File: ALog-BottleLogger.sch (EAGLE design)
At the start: 98 parts, among them IC2 ATMEGA644M, J6 5.5x2.1mm Barrel, Q1 220mA/50V/3.5Ω, Q4 4.3A/20V/54mΩ, Q5 4.3A/20V/54mΩ, Q6 4.3A/20V/54mΩ, Q7 4.3A/20V/54mΩ, Q8 220mA/50V/3.5Ω, Q9 220mA/50V/3.5Ω, U2 FT231X-Q

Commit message: fully routed, looking for review
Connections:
- net +3V3: no longer J14.2
- net 1.8V_REF: no longer J14.1
- net ADC10: now also J14.10; no longer J15.2
- net ADC11: now also J14.9; no longer J15.1
- net ADC12: now also J14.5; no longer J14.7
- net ADC13: now also J14.4; no longer J14.6
- net ADC8: now also J15.5; no longer J15.7
- net ADC9: now also J15.4; no longer J15.6
- net BATT+: now also J2.9
- net D15~: now also J2.8; no longer J2.10
- net D3~: now also J2.6; no longer J2.8
- net EXT_3.3V: now also J14.2, J14.7, J15.2, J15.7, J2.4; no longer J14.4, J14.9, J15.4, J15.9, J2.6
- net EXT_5V: now also J14.8, J15.8, J2.5; no longer J14.10, J15.10, J2.7
- net EXT_5V1: now also J14.3, J15.3; no longer J14.5, J15.5
- net GND: now also J14.1, J14.6, J15.1, J15.6, J2.10, J2.3; no longer J14.3, J14.8, J15.3, J15.8, J2.5
- net MCU_ADC0: now also J2.7; no longer J2.9
- net MISO/D6: now also J15.10; no longer J2.2
- net MOSI/D5: now also J2.1; no longer J2.3
- net SCK/D7: now also J15.9; no longer J2.1
- net SS/D4: now also J2.2; no longer J2.4

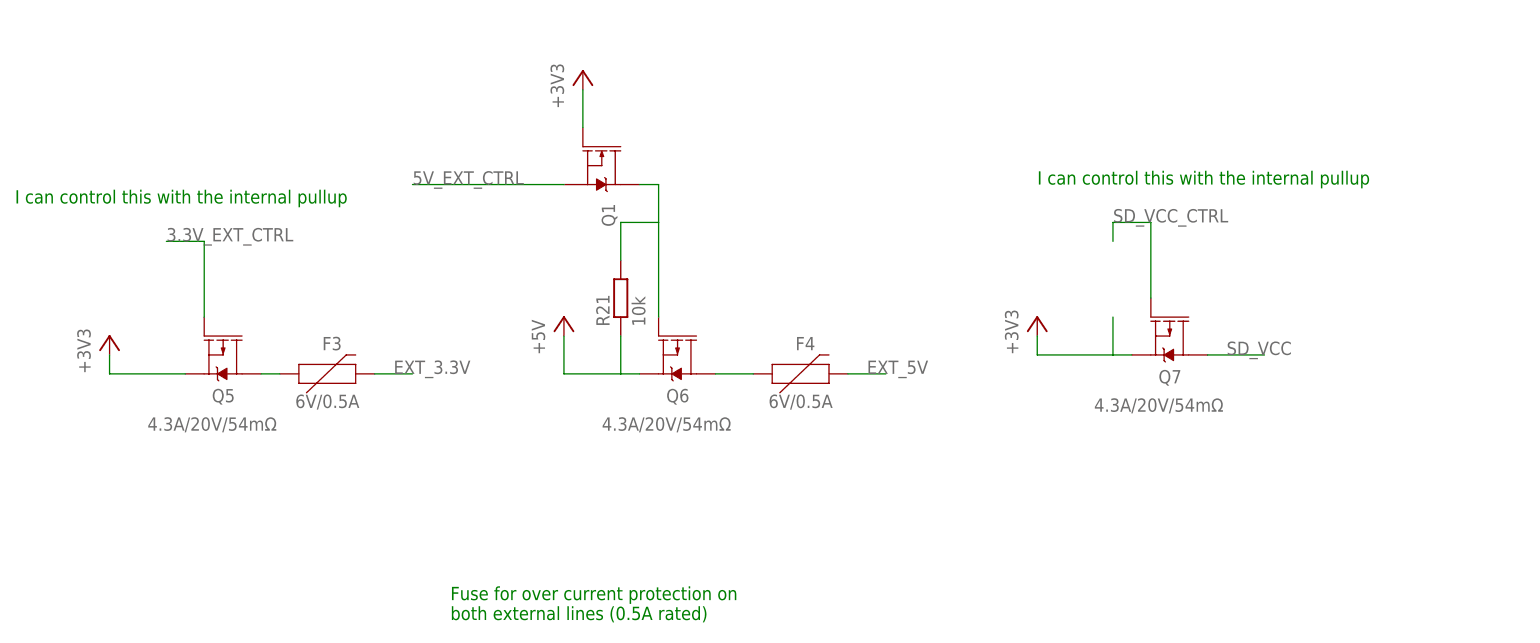
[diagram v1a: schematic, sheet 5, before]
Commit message: Add 10K pull downs on mosphets for external controls
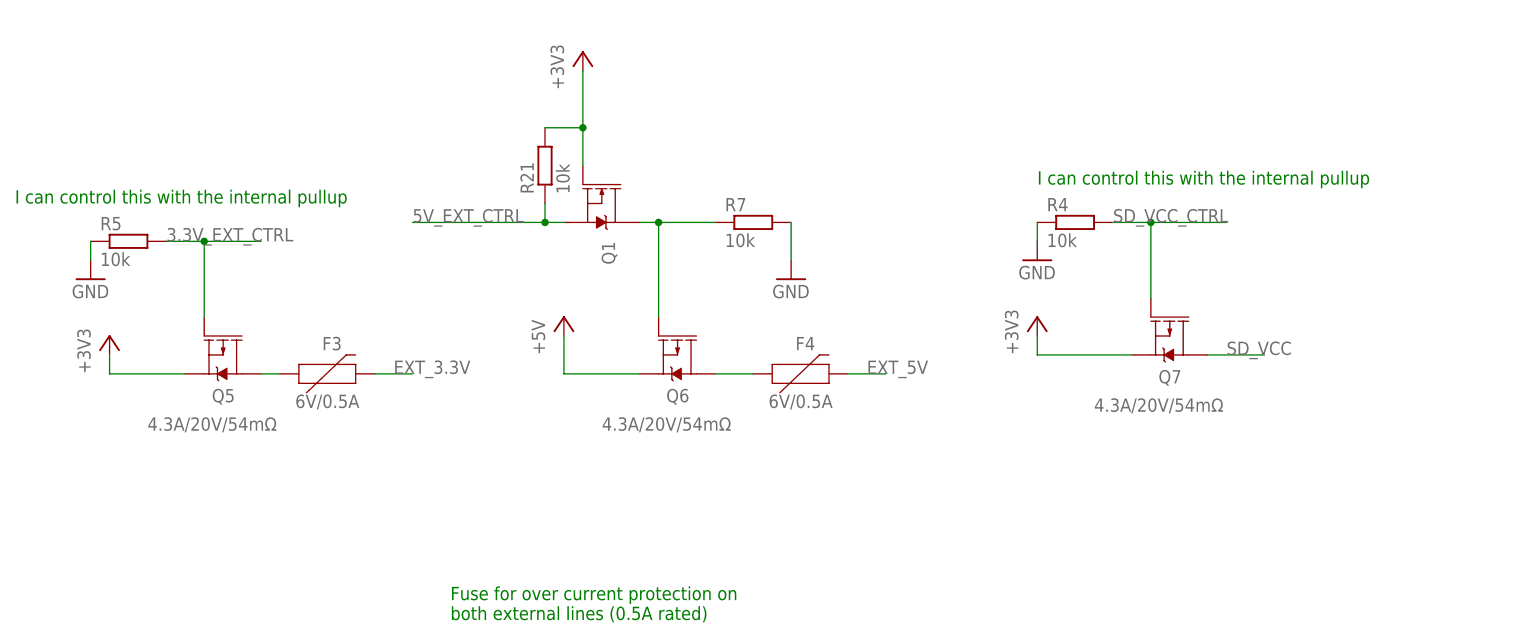
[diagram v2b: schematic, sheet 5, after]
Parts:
- added R4, R5, R7: 10k, rcl:R-EU_R0603
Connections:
- net +3V3: now also R21.2
- net +5V: no longer R21.1
- net 3.3V_EXT_CTRL: now also R5.2
- net 5V_EXT_CTRL: now also R21.1
- net GND: now also R7.2
- net SDA_HV: now also R7.1; no longer R21.2
- net SD_VCC_CTRL: now also R4.2
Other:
- moved on the sheet: Q1, R21
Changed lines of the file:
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@@
 <part name="R_LED1" library="resistor" deviceset="R-US_" device="R0603" value="220"/>
 <part name="GND11" library="supply1" deviceset="GND" device=""/>
+<part name="R4" library="rcl" deviceset="R-EU_" device="R0603" value="10k"/>
+<part name="R5" library="rcl" deviceset="R-EU_" device="R0603" value="10k"/>
+<part name="GND13" library="supply1" deviceset="GND" device=""/>
+<part name="GND14" library="supply1" deviceset="GND" device=""/>
+<part name="GND17" library="supply1" deviceset="GND" device=""/>
+<part name="R7" library="rcl" deviceset="R-EU_" device="R0603" value="10k"/>
 </parts>
 <sheets>
@@
 <attribute name="VALUE" x="58.42" y="27.94" size="1.778" layer="96" font="vector"/>
 </instance>
-<instance part="R21" gate="G$1" x="60.96" y="45.72" rot="R90"/>
+<instance part="R21" gate="G$1" x="50.8" y="63.5" rot="R90"/>
 <instance part="F3" gate="G$1" x="20.32" y="35.56"/>
 <instance part="F4" gate="G$1" x="83.82" y="35.56"/>
 <instance part="P+1" gate="1" x="53.34" y="43.18"/>
-<instance part="Q1" gate="NMOS" x="58.42" y="63.5" smashed="yes" rot="R270">
-<attribute name="NAME" x="58.42" y="58.42" size="1.778" layer="95" font="vector" rot="R270"/>
+<instance part="Q1" gate="NMOS" x="58.42" y="58.42" smashed="yes" rot="R270">
+<attribute name="NAME" x="58.42" y="53.34" size="1.778" layer="95" font="vector" rot="R270"/>
 </instance>
-<instance part="+3V12" gate="G$1" x="55.88" y="76.2"/>
+<instance part="+3V12" gate="G$1" x="55.88" y="78.74"/>
 <instance part="+3V13" gate="G$1" x="116.84" y="43.18"/>
 <instance part="+3V14" gate="G$1" x="-7.62" y="40.64"/>
+<instance part="R4" gate="G$1" x="121.92" y="55.88"/>
+<instance part="R5" gate="G$1" x="-5.08" y="53.34"/>
+<instance part="GND13" gate="1" x="-10.16" y="48.26"/>
+<instance part="GND14" gate="1" x="116.84" y="50.8"/>
+<instance part="GND17" gate="1" x="83.82" y="48.26"/>
+<instance part="R7" gate="G$1" x="78.74" y="55.88"/>
 </instances>
 <busses>
@@
 <net name="SD_VCC_CTRL" class="0">
 <segment>
-<wire x1="127" y1="53.34" x2="127" y2="55.88" width="0.1524" layer="91"/>
 <pinref part="Q7" gate="G$1" pin="G"/>
 <wire x1="127" y1="55.88" x2="132.08" y2="55.88" width="0.1524" layer="91"/>
 <wire x1="132.08" y1="55.88" x2="132.08" y2="45.72" width="0.1524" layer="91"/>
 <label x="127" y="55.88" size="1.778" layer="95"/>
+<pinref part="R4" gate="G$1" pin="2"/>
+<wire x1="132.08" y1="55.88" x2="142.24" y2="55.88" width="0.1524" layer="91"/>
+<junction x="132.08" y="55.88"/>
 </segment>
 </net>
@@
 <wire x1="5.08" y1="53.34" x2="5.08" y2="43.18" width="0.1524" layer="91"/>
 <label x="0" y="53.34" size="1.778" layer="95"/>
+<pinref part="R5" gate="G$1" pin="2"/>
+<wire x1="5.08" y1="53.34" x2="12.7" y2="53.34" width="0.1524" layer="91"/>
+<junction x="5.08" y="53.34"/>
 </segment>
 </net>
@@
 <segment>
 <pinref part="Q6" gate="G$1" pin="S"/>
-<wire x1="63.5" y1="35.56" x2="60.96" y2="35.56" width="0.1524" layer="91"/>
-<pinref part="R21" gate="G$1" pin="1"/>
-<wire x1="60.96" y1="35.56" x2="53.34" y2="35.56" width="0.1524" layer="91"/>
+<wire x1="63.5" y1="35.56" x2="53.34" y2="35.56" width="0.1524" layer="91"/>
 <wire x1="53.34" y1="35.56" x2="53.34" y2="40.64" width="0.1524" layer="91"/>
-<wire x1="60.96" y1="40.64" x2="60.96" y2="35.56" width="0.1524" layer="91"/>
 <pinref part="P+1" gate="1" pin="+5V"/>
 </segment>
@@
 <segment>
 <pinref part="Q1" gate="NMOS" pin="D"/>
-<wire x1="63.5" y1="60.96" x2="66.04" y2="60.96" width="0.1524" layer="91"/>
+<wire x1="63.5" y1="55.88" x2="66.04" y2="55.88" width="0.1524" layer="91"/>
 <pinref part="Q6" gate="G$1" pin="G"/>
-<wire x1="66.04" y1="60.96" x2="66.04" y2="55.88" width="0.1524" layer="91"/>
+<wire x1="66.04" y1="55.88" x2="66.04" y2="43.18" width="0.1524" layer="91"/>
+<junction x="66.04" y="55.88"/>
+<pinref part="R7" gate="G$1" pin="1"/>
+<wire x1="66.04" y1="55.88" x2="73.66" y2="55.88" width="0.1524" layer="91"/>
+</segment>
+</net>
+<net name="+3V3" class="0">
+<segment>
+<pinref part="Q1" gate="NMOS" pin="G"/>
+<wire x1="55.88" y1="76.2" x2="55.88" y2="68.58" width="0.1524" layer="91"/>
+<pinref part="+3V12" gate="G$1" pin="+3V3"/>
 <pinref part="R21" gate="G$1" pin="2"/>
-<wire x1="66.04" y1="55.88" x2="66.04" y2="43.18" width="0.1524" layer="91"/>
-<wire x1="60.96" y1="50.8" x2="60.96" y2="55.88" width="0.1524" layer="91"/>
-<wire x1="60.96" y1="55.88" x2="66.04" y2="55.88" width="0.1524" layer="91"/>
-</segment>
-</net>
-<net name="+3V3" class="0">
-<segment>
-<pinref part="Q1" gate="NMOS" pin="G"/>
-<wire x1="55.88" y1="73.66" x2="55.88" y2="68.58" width="0.1524" layer="91"/>
-<pinref part="+3V12" gate="G$1" pin="+3V3"/>
+<wire x1="55.88" y1="68.58" x2="55.88" y2="63.5" width="0.1524" layer="91"/>
+<wire x1="50.8" y1="68.58" x2="55.88" y2="68.58" width="0.1524" layer="91"/>
+<junction x="55.88" y="68.58"/>
 </segment>
 <segment>
 <pinref part="Q7" gate="G$1" pin="S"/>
-<wire x1="129.54" y1="38.1" x2="127" y2="38.1" width="0.1524" layer="91"/>
-<wire x1="127" y1="38.1" x2="116.84" y2="38.1" width="0.1524" layer="91"/>
-<wire x1="127" y1="43.18" x2="127" y2="38.1" width="0.1524" layer="91"/>
+<wire x1="129.54" y1="38.1" x2="116.84" y2="38.1" width="0.1524" layer="91"/>
 <wire x1="116.84" y1="40.64" x2="116.84" y2="38.1" width="0.1524" layer="91"/>
 <pinref part="+3V13" gate="G$1" pin="+3V3"/>
@@
 <segment>
 <pinref part="Q1" gate="NMOS" pin="S"/>
-<wire x1="53.34" y1="60.96" x2="33.02" y2="60.96" width="0.1524" layer="91"/>
-<label x="33.02" y="60.96" size="1.778" layer="95"/>
-</segment>
-</net>
+<wire x1="53.34" y1="55.88" x2="50.8" y2="55.88" width="0.1524" layer="91"/>
+<label x="33.02" y="55.88" size="1.778" layer="95"/>
+<pinref part="R21" gate="G$1" pin="1"/>
+<wire x1="50.8" y1="55.88" x2="33.02" y2="55.88" width="0.1524" layer="91"/>
+<wire x1="50.8" y1="58.42" x2="50.8" y2="55.88" width="0.1524" layer="91"/>
+<junction x="50.8" y="55.88"/>
+</segment>
+</net>
+<net name="GND" class="0">
+<segment>
+<pinref part="GND13" gate="1" pin="GND"/>
+<wire x1="-10.16" y1="53.34" x2="-10.16" y2="50.8" width="0.1524" layer="91"/>
+</segment>
+<segment>
+<pinref part="GND14" gate="1" pin="GND"/>
+<wire x1="116.84" y1="55.88" x2="116.84" y2="53.34" width="0.1524" layer="91"/>
+</segment>
+<segment>
+<pinref part="GND17" gate="1" pin="GND"/>
+<pinref part="R7" gate="G$1" pin="2"/>
+<wire x1="83.82" y1="55.88" x2="83.82" y2="50.8" width="0.1524" layer="91"/>
+</segment>
+</net>

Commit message: Fixed 5V control and a few other things, fully routed and ready for review
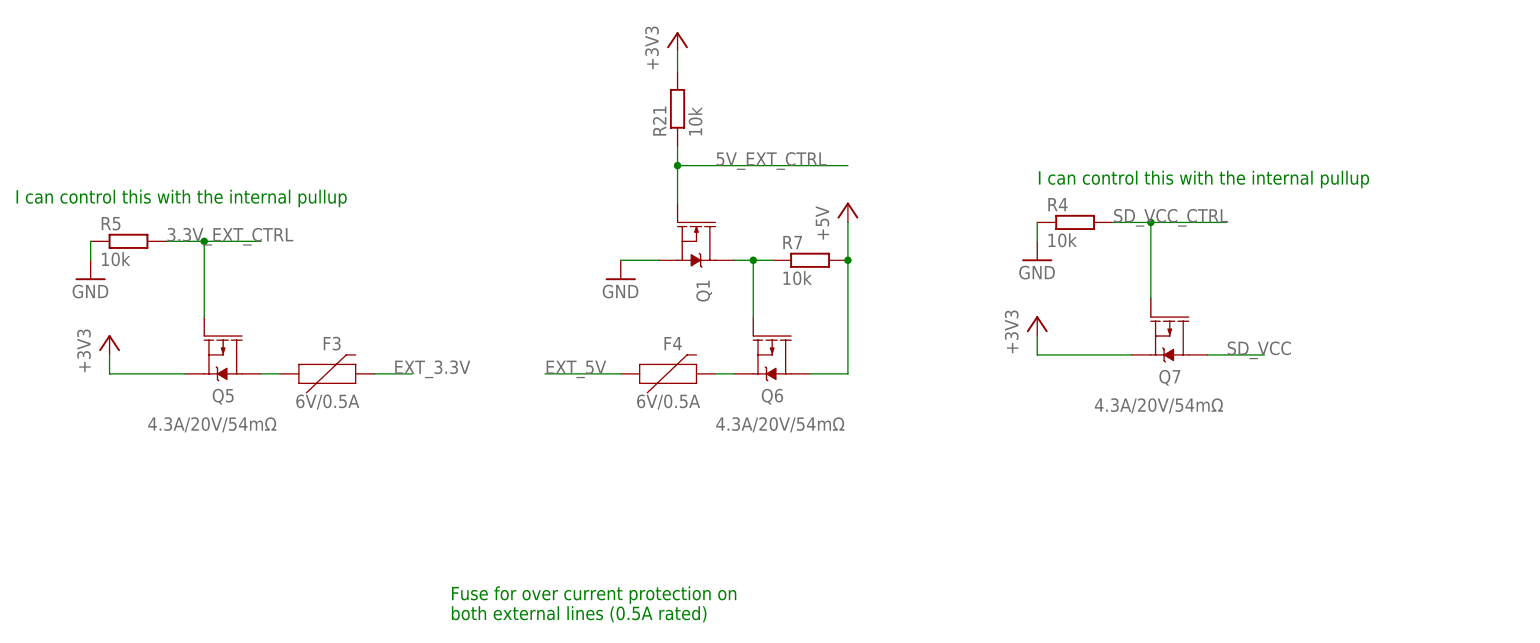
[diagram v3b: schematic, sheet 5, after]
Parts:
- removed J6: 5.5x2.1mm Barrel, SparkFun-Connectors:POWER_JACKSMD
- removed Q4: 4.3A/20V/54mΩ, SparkFun-DiscreteSemi:MOSFET_PCH-IRLML2244
- added Q11: 220mA/50V/3.5Ω, SparkFun-DiscreteSemi:MOSFET-NCH-BSS138
- added Q12: 4.3A/20V/54mΩ, SparkFun-DiscreteSemi:MOSFET_PCH-IRLML2244
- added R14: 10k, rcl:R-EU_R0603
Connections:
- net MISO renamed MISO/D5
- net MOSI renamed MOSI/D6
- removed net D1: IC2.(PCINT9/CLKO/T1)PB1
- removed net EXT_5V1: J14.3, J15.3, J16.8, J8.8
- removed net N$23: F4.1, Q6.D
- removed net SCK: SD.SCLK
- new net N$11: Q11.G, Q12.S, R14.2
- new net N$14: F4.2, Q6.S
- new net N$6: Q1.D, Q6.G, R7.1
- new net RTC_EN: IC2.(PCINT9/CLKO/T1)PB1, RTC1.VCC
- net +3V3: no longer Q1.G, RTC1.VCC
- net +5V: now also Q11.D, Q6.D, R14.1, R7.2; no longer MICRO_USB.VDD, Q4.S, Q6.S
- net 5V_EXT_CTRL: now also Q1.G; no longer Q1.S
- net BATT+: no longer J6.PWR
- net EXT_5V: now also F4.1, J14.3, J15.3, J16.8, J8.8; no longer F4.2
- net GND: now also Q1.S, Q12.D, R4.1, R5.1; no longer J6.GND, J6.GNDBREAK, R7.2
- net SCK/D7: now also SD.SCLK
- net SDA_HV: no longer Q1.D, Q6.G, R7.1
- net VUSB: now also MICRO_USB.VDD, Q11.S, Q12.G; no longer Q4.D, Q4.G
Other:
- note removed: "Add Mosphet control for FTDI"
- note removed: "Power In (From battery)"
- moved on the sheet: F4, MICRO_USB, Q1, Q6, R21, R7
